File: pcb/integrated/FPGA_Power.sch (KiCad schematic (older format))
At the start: 28 parts, among them U3001 XC7S25-L1FTGB196

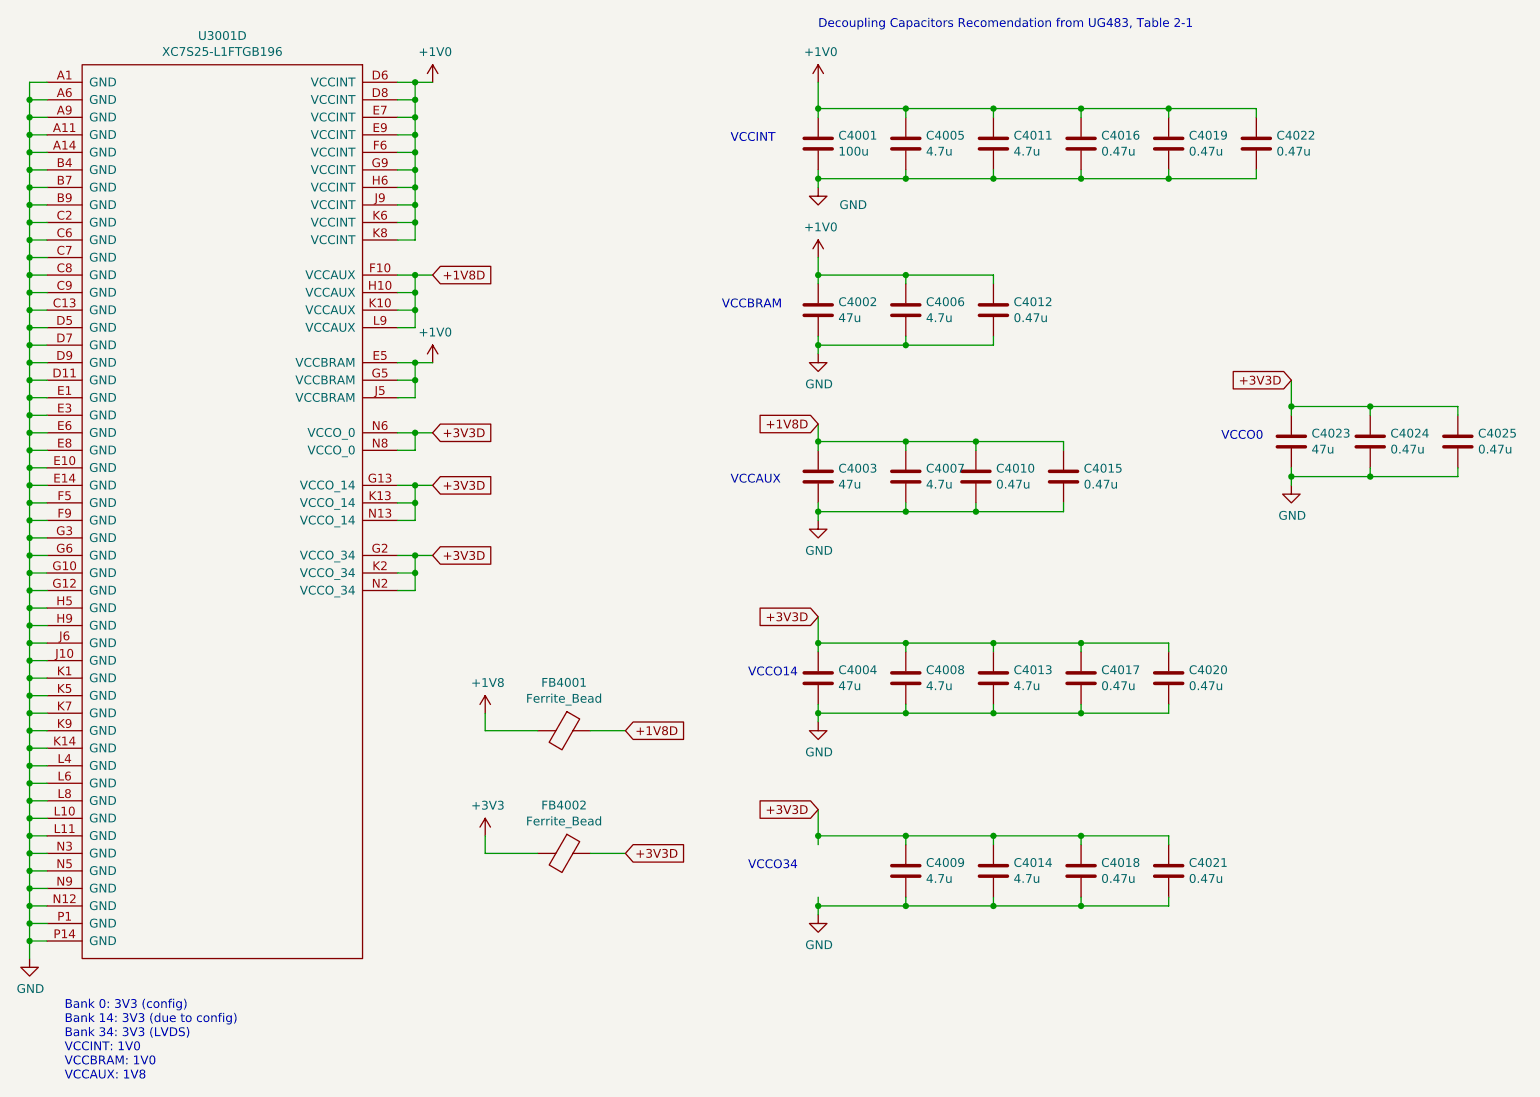
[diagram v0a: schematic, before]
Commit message: schematic fixes and component placement
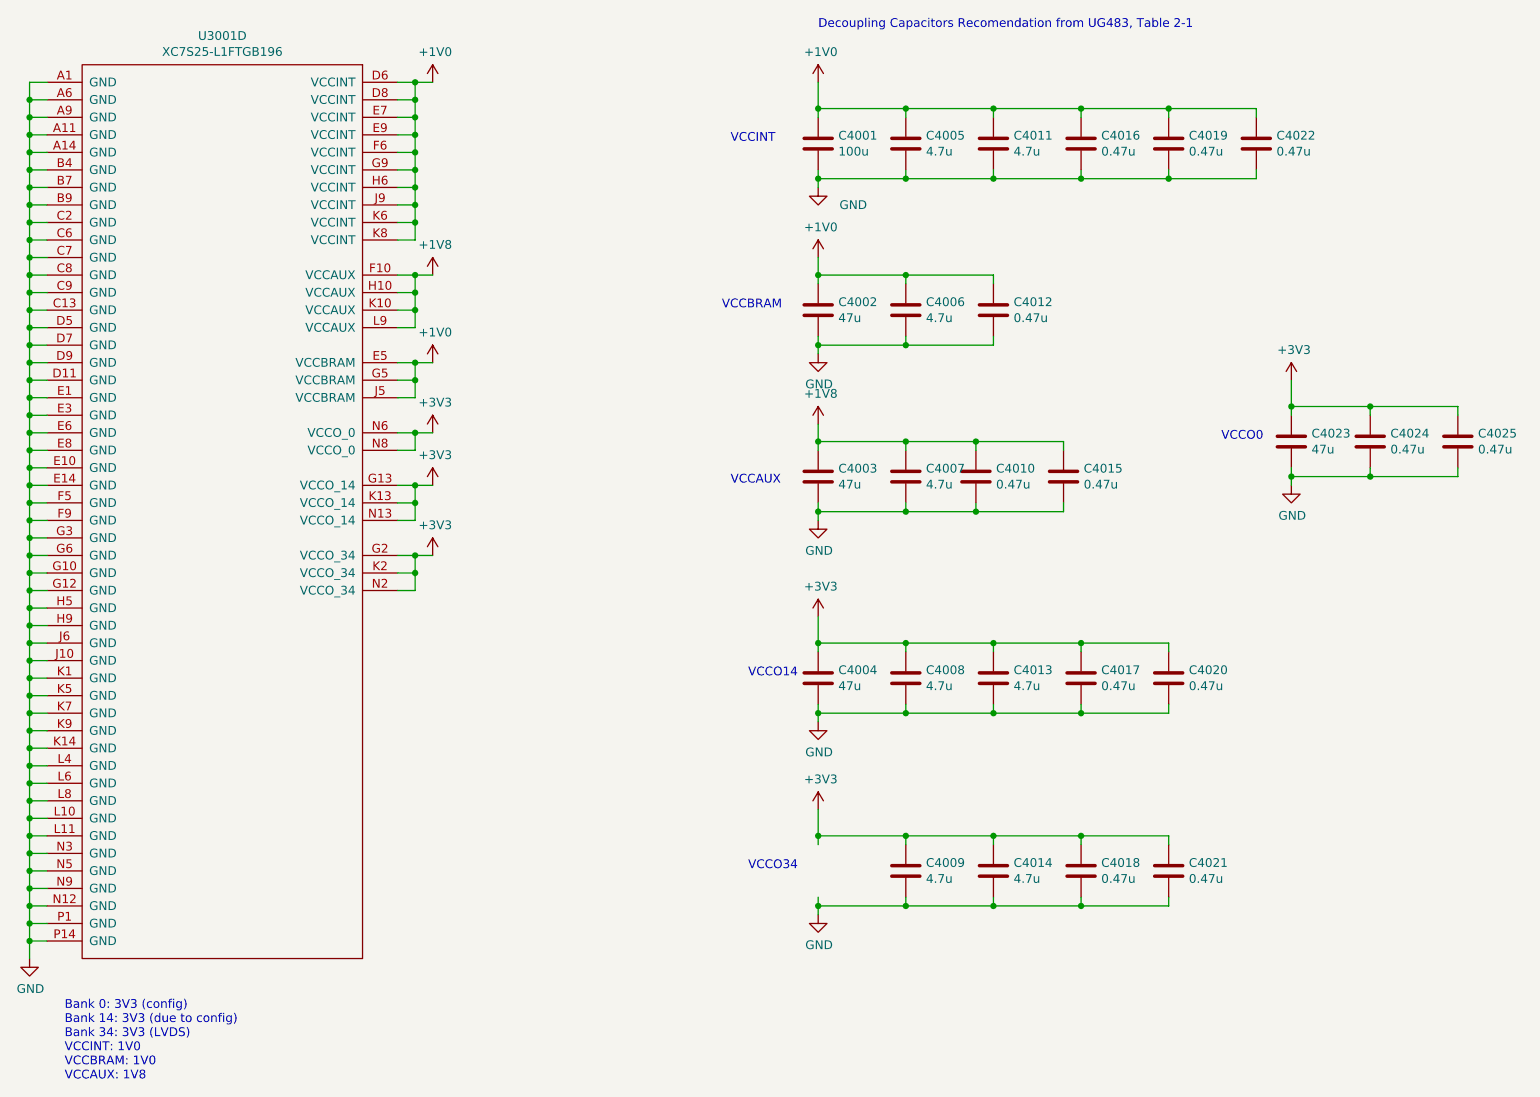
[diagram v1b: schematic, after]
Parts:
- removed FB4001, FB4002: Ferrite_Bead, Inductor_SMD:L_0805_2012Metric, symbol Device:Ferrite_Bead
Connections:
- net +1V8D is gone; now on net +1V8: C4003.1, C4007.1, C4010.1, C4015.1, U3001.F10 (VCCAUX), U3001.H10 (VCCAUX), U3001.K10 (VCCAUX), U3001.L9 (VCCAUX)
- net +3V3D is gone; now on net +3V3: C4004.1, C4008.1, C4009.1, C4013.1, C4014.1, C4017.1, C4018.1, C4020.1, C4021.1, C4023.1, C4024.1, C4025.1, U3001.G13 (VCCO_14), U3001.G2 (VCCO_34), U3001.K13 (VCCO_14), U3001.K2 (VCCO_34), U3001.N13 (VCCO_14), U3001.N2 (VCCO_34), U3001.N6 (VCCO_0), U3001.N8 (VCCO_0)
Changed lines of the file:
@@
-$EndComp
-$Comp
-L power:+1V8 #PWR04004
-U 1 1 5C2938DC
-P 4700 4800
-F 0 "#PWR04004" H 4700 4650 50  0001 C CNN
-F 1 "+1V8" H 4715 4973 50  0000 C CNN
-F 2 "" H 4700 4800 50  0001 C CNN
-F 3 "" H 4700 4800 50  0001 C CNN
-	1    4700 4800
-	1    0    0    -1
 $EndComp
 $Comp
@@
 	1    0    0    -1
 $EndComp
-$Comp
-L power:+3V3 #PWR04005
-U 1 1 5C42A22F
-P 4700 5500
-F 0 "#PWR04005" H 4700 5350 50  0001 C CNN
-F 1 "+3V3" H 4715 5673 50  0000 C CNN
-F 2 "" H 4700 5500 50  0001 C CNN
-F 3 "" H 4700 5500 50  0001 C CNN
-	1    4700 5500
-	1    0    0    -1
-$EndComp
 Wire Wire Line
 	8600 5900 8600 5850
@@
 	1    0    0    -1
 $EndComp
-Text GLabel 6600 5350 0    50   Input ~ 0
-+3V3D
-Text GLabel 6600 4250 0    50   Input ~ 0
-+3V3D
-Text GLabel 4400 3900 2    50   Input ~ 0
-+3V3D
-Text GLabel 4400 3500 2    50   Input ~ 0
-+3V3D
-Text GLabel 4400 3200 2    50   Input ~ 0
-+3V3D
-Text GLabel 9300 2900 0    50   Input ~ 0
-+3V3D
-Text GLabel 6600 3150 0    50   Input ~ 0
-+1V8D
-Text GLabel 4400 2300 2    50   Input ~ 0
-+1V8D
-$Comp
-L Device:Ferrite_Bead FB4001
-U 1 1 5C693AA4
-P 5150 4900
-F 0 "FB4001" V 4876 4900 50  0000 C CNN
-F 1 "Ferrite_Bead" V 4967 4900 50  0000 C CNN
-F 2 "Inductor_SMD:L_0805_2012Metric" V 5080 4900 50  0001 C CNN
-F 3 "~" H 5150 4900 50  0001 C CNN
-	1    5150 4900
-	0    1    1    0
-$EndComp
-$Comp
-L Device:Ferrite_Bead FB4002
-U 1 1 5C693BE0
-P 5150 5600
-F 0 "FB4002" V 4876 5600 50  0000 C CNN
-F 1 "Ferrite_Bead" V 4967 5600 50  0000 C CNN
-F 2 "Inductor_SMD:L_0805_2012Metric" V 5080 5600 50  0001 C CNN
-F 3 "~" H 5150 5600 50  0001 C CNN
-	1    5150 5600
-	0    1    1    0
-$EndComp
-Text GLabel 5500 5600 2    50   Input ~ 0
-+3V3D
-Text GLabel 5500 4900 2    50   Input ~ 0
-+1V8D
-Wire Wire Line
-	4700 4800 4700 4900
-Wire Wire Line
-	4700 4900 5000 4900
-Wire Wire Line
-	4700 5500 4700 5600
-Wire Wire Line
-	4700 5600 5000 5600
-Wire Wire Line
-	5300 4900 5500 4900
-Wire Wire Line
-	5300 5600 5500 5600
+$Comp
+L power:+1V8 #PWR0165
+U 1 1 5D7FCDEC
+P 4400 2300
+F 0 "#PWR0165" H 4400 2150 50  0001 C CNN
+F 1 "+1V8" H 4415 2473 50  0000 C CNN
+F 2 "" H 4400 2300 50  0001 C CNN
+F 3 "" H 4400 2300 50  0001 C CNN
+	1    4400 2300
+	1    0    0    -1
+$EndComp
+$Comp
+L power:+3V3 #PWR0166
+U 1 1 5D7FD9B0
+P 4400 3200
+F 0 "#PWR0166" H 4400 3050 50  0001 C CNN
+F 1 "+3V3" H 4415 3373 50  0000 C CNN
+F 2 "" H 4400 3200 50  0001 C CNN
+F 3 "" H 4400 3200 50  0001 C CNN
+	1    4400 3200
+	1    0    0    -1
+$EndComp
+$Comp
+L power:+3V3 #PWR0167
+U 1 1 5D7FDF8B
+P 4400 3500
+F 0 "#PWR0167" H 4400 3350 50  0001 C CNN
+F 1 "+3V3" H 4415 3673 50  0000 C CNN
+F 2 "" H 4400 3500 50  0001 C CNN
+F 3 "" H 4400 3500 50  0001 C CNN
+	1    4400 3500
+	1    0    0    -1
+$EndComp
+$Comp
+L power:+3V3 #PWR0168
+U 1 1 5D7FE5DC
+P 4400 3900
+F 0 "#PWR0168" H 4400 3750 50  0001 C CNN
+F 1 "+3V3" H 4415 4073 50  0000 C CNN
+F 2 "" H 4400 3900 50  0001 C CNN
+F 3 "" H 4400 3900 50  0001 C CNN
+	1    4400 3900
+	1    0    0    -1
+$EndComp
+$Comp
+L power:+1V8 #PWR0169
+U 1 1 5D7FEB39
+P 6600 3150
+F 0 "#PWR0169" H 6600 3000 50  0001 C CNN
+F 1 "+1V8" H 6615 3323 50  0000 C CNN
+F 2 "" H 6600 3150 50  0001 C CNN
+F 3 "" H 6600 3150 50  0001 C CNN
+	1    6600 3150
+	1    0    0    -1
+$EndComp
+$Comp
+L power:+3V3 #PWR0170
+U 1 1 5D7FF38C
+P 6600 4250
+F 0 "#PWR0170" H 6600 4100 50  0001 C CNN
+F 1 "+3V3" H 6615 4423 50  0000 C CNN
+F 2 "" H 6600 4250 50  0001 C CNN
+F 3 "" H 6600 4250 50  0001 C CNN
+	1    6600 4250
+	1    0    0    -1
+$EndComp
+$Comp
+L power:+3V3 #PWR0171
+U 1 1 5D7FFA68
+P 6600 5350
+F 0 "#PWR0171" H 6600 5200 50  0001 C CNN
+F 1 "+3V3" H 6615 5523 50  0000 C CNN
+F 2 "" H 6600 5350 50  0001 C CNN
+F 3 "" H 6600 5350 50  0001 C CNN
+	1    6600 5350
+	1    0    0    -1
+$EndComp
+$Comp
+L power:+3V3 #PWR0172
+U 1 1 5D7FFF0B
+P 9300 2900
+F 0 "#PWR0172" H 9300 2750 50  0001 C CNN
+F 1 "+3V3" H 9315 3073 50  0000 C CNN
+F 2 "" H 9300 2900 50  0001 C CNN
+F 3 "" H 9300 2900 50  0001 C CNN
+	1    9300 2900
+	1    0    0    -1
+$EndComp
 $EndSCHEMATC

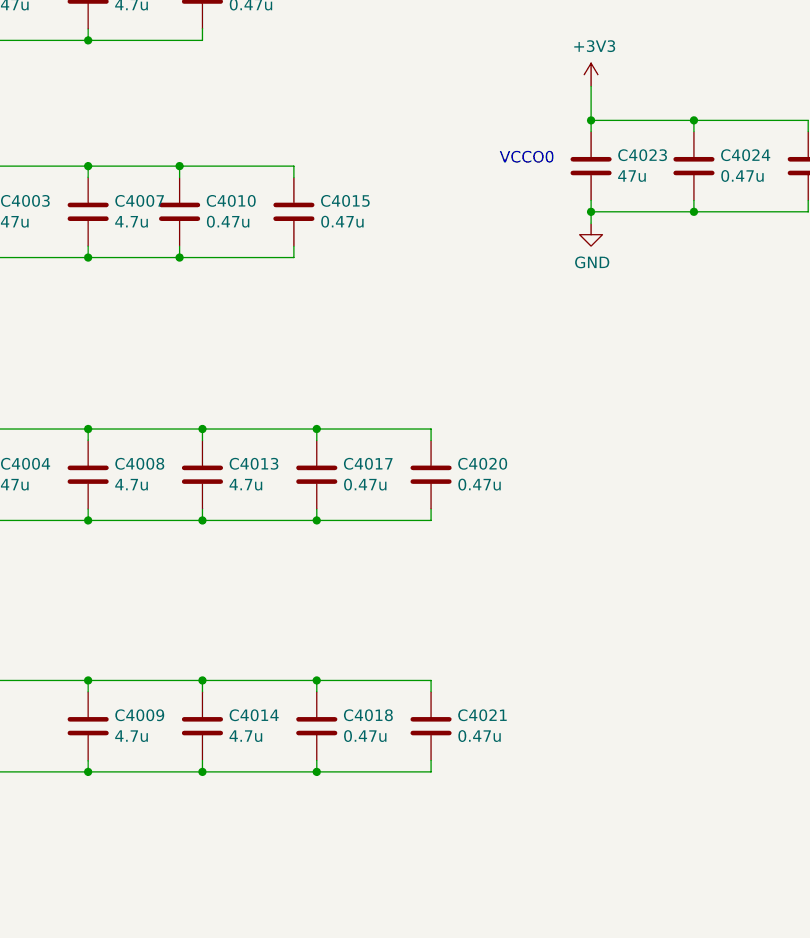
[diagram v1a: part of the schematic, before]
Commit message: routing, all componens placed on PCB
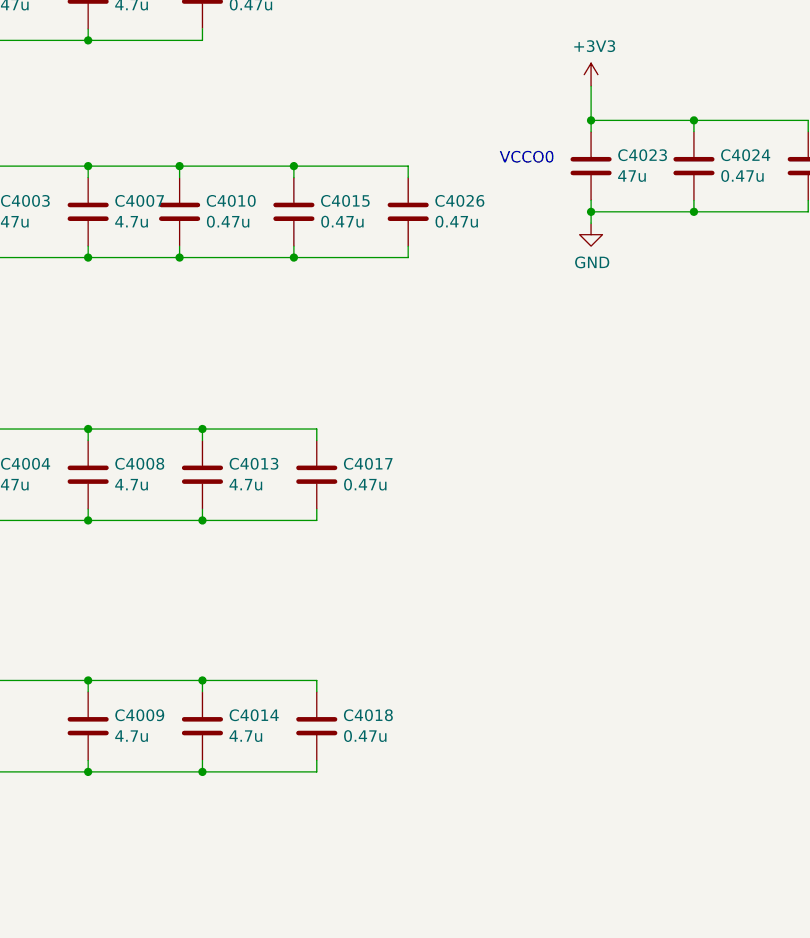
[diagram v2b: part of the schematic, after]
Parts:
- removed C4020, C4021: 0.47u, Capacitor_SMD:C_0402_1005Metric, symbol Device:C
- added C4026: 0.47u, Capacitor_SMD:C_0402_1005Metric, symbol Device:C
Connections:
- net +1V8: now also C4026.1
- net GND: now also C4026.2
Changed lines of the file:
@@
-	1    0    0    -1
-$EndComp
-Wire Wire Line
-	8600 5900 8600 5850
-Connection ~ 8100 5900
-Wire Wire Line
-	8100 5900 8600 5900
-Wire Wire Line
-	8600 5500 8600 5550
-Connection ~ 8100 5500
-Wire Wire Line
-	8100 5500 8600 5500
-Wire Wire Line
-	8600 4800 8600 4750
-Connection ~ 8100 4800
-Wire Wire Line
-	8100 4800 8600 4800
-Wire Wire Line
-	8600 4400 8600 4450
-Connection ~ 8100 4400
-Wire Wire Line
-	8100 4400 8600 4400
-$Comp
-L Device:C C4020
-U 1 1 5C6484C1
-P 8600 4600
-F 0 "C4020" H 8715 4646 50  0000 L CNN
-F 1 "0.47u" H 8715 4555 50  0000 L CNN
-F 2 "Capacitor_SMD:C_0402_1005Metric" H 8638 4450 50  0001 C CNN
-F 3 "~" H 8600 4600 50  0001 C CNN
-	1    8600 4600
-	1    0    0    -1
-$EndComp
-$Comp
-L Device:C C4021
-U 1 1 5C6486F5
-P 8600 5700
-F 0 "C4021" H 8715 5746 50  0000 L CNN
-F 1 "0.47u" H 8715 5655 50  0000 L CNN
-F 2 "Capacitor_SMD:C_0402_1005Metric" H 8638 5550 50  0001 C CNN
-F 3 "~" H 8600 5700 50  0001 C CNN
-	1    8600 5700
 	1    0    0    -1
 $EndComp
@@
 	1    0    0    -1
 $EndComp
+$Comp
+L Device:C C4026
+U 1 1 5DE33B48
+P 8500 3450
+F 0 "C4026" H 8615 3496 50  0000 L CNN
+F 1 "0.47u" H 8615 3405 50  0000 L CNN
+F 2 "Capacitor_SMD:C_0402_1005Metric" H 8538 3300 50  0001 C CNN
+F 3 "~" H 8500 3450 50  0001 C CNN
+	1    8500 3450
+	1    0    0    -1
+$EndComp
+Wire Wire Line
+	8000 3250 8500 3250
+Wire Wire Line
+	8500 3250 8500 3300
+Connection ~ 8000 3250
+Wire Wire Line
+	8000 3650 8500 3650
+Wire Wire Line
+	8500 3650 8500 3600
+Connection ~ 8000 3650
 $EndSCHEMATC
